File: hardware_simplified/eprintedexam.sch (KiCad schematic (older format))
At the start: 47 parts, among them J1 Conn_01x04, J2 Conn_01x08, Q1 2N7002, Q2 2N7002, Q3 2N7002, Q4 2N7002, Q5 2N7002, Q6 2N7002, SW1 SW_Push, SW2 SW_Push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

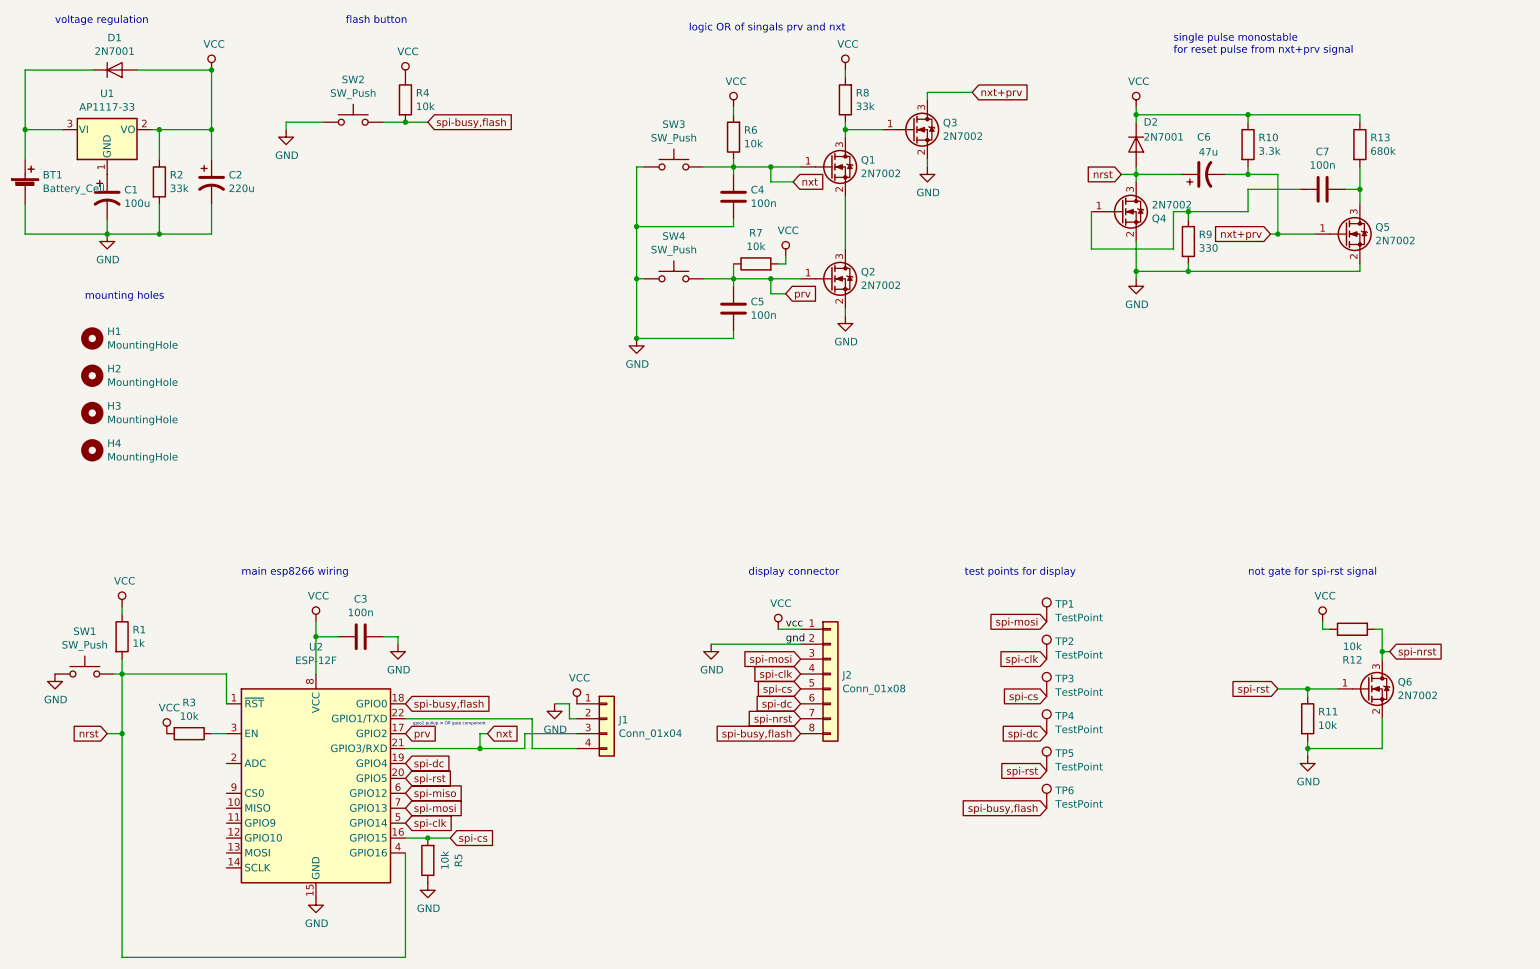
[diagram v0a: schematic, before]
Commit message: fixed monostable and improved pcb layout
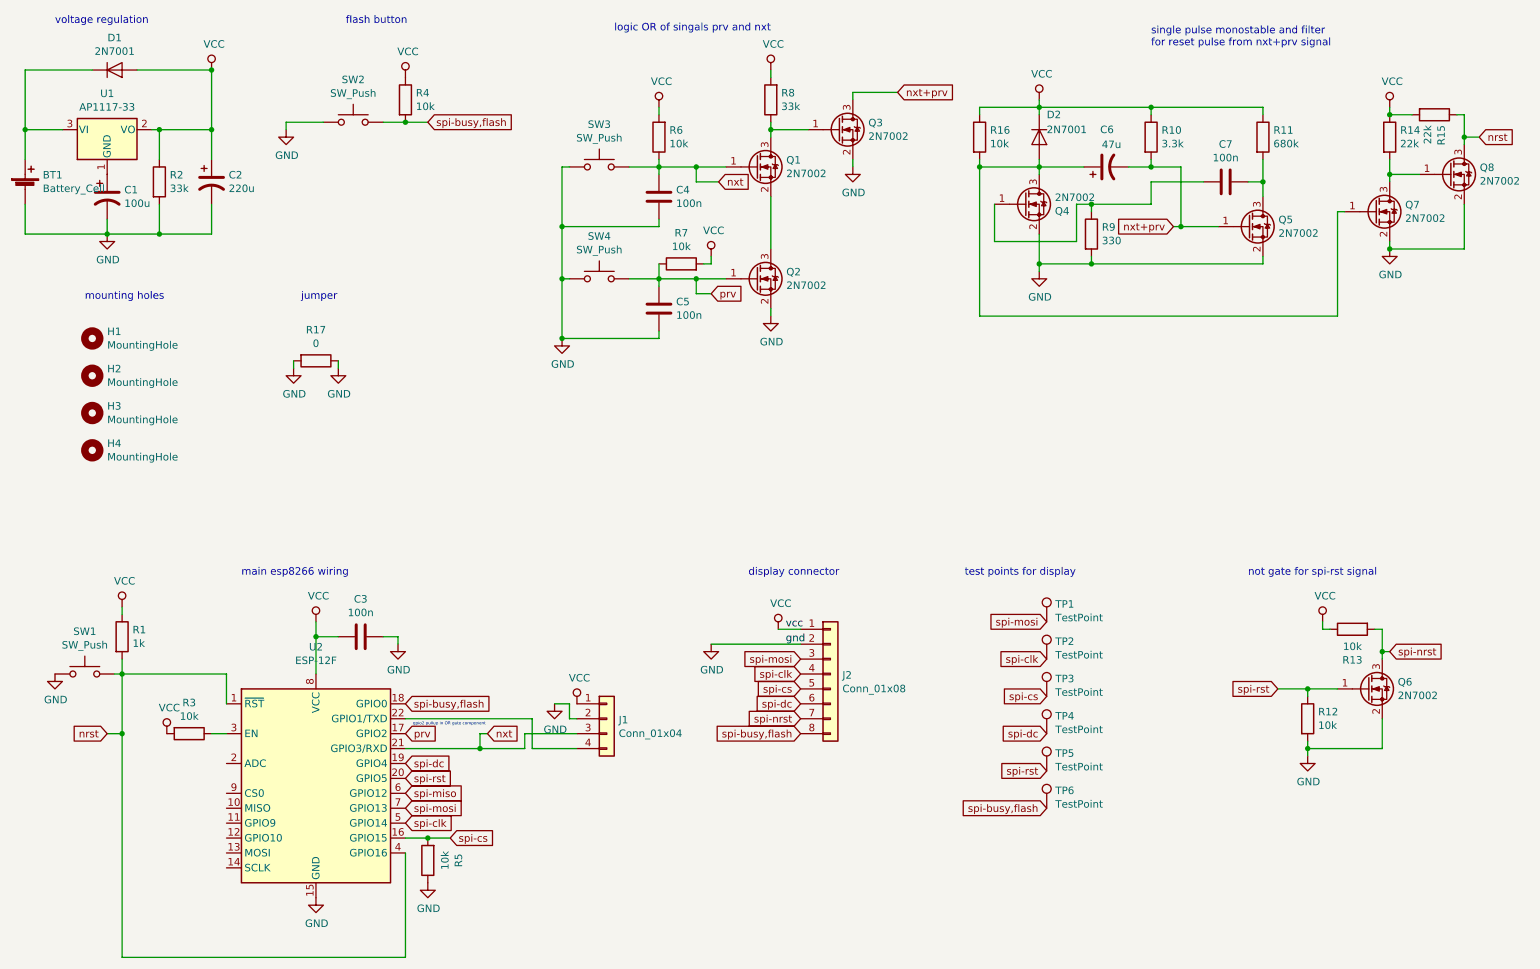
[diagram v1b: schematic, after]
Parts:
- added Q7, Q8: 2N7002, Package_TO_SOT_SMD:SOT-23, symbol Transistor_FET:2N7002
- added R14, R15: 22k, Resistor_SMD:R_1206_3216Metric, symbol Device:R
- added R16: 10k, Resistor_THT:R_Axial_DIN0207_L6.3mm_D2.5mm_P10.16mm_Horizontal, symbol Device:R
- added R17: 0, Resistor_SMD:R_1206_3216Metric, symbol Device:R
- renumbered R13 to R11, R11 to R12, R12 to R13
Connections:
- net GND: now also Q7.2 (S), Q8.2 (S), R17.1, R17.2
- net VCC: now also R14.1, R15.2, R16.1
- net nrst: now also Q8.3 (D), R15.1; no longer C6.1, D2.2 (A), Q4.3 (D)
- new net: C6.1, D2.2 (A), Q4.3 (D), Q7.1 (G), R16.2
- new net: Q7.3 (D), Q8.1 (G), R14.2
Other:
- note added: "jumper"
- note added: "single pulse monostable and filter\nfor reset pulse from nxt+prv signal"
- note removed: "single pulse monostable\nfor reset pulse from nxt+prv signal"
- moved on the sheet: C4, C5, C6, C7, D2, Q1, Q2, Q3, Q4, Q5, R10, R11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

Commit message: changed nxt and prv port
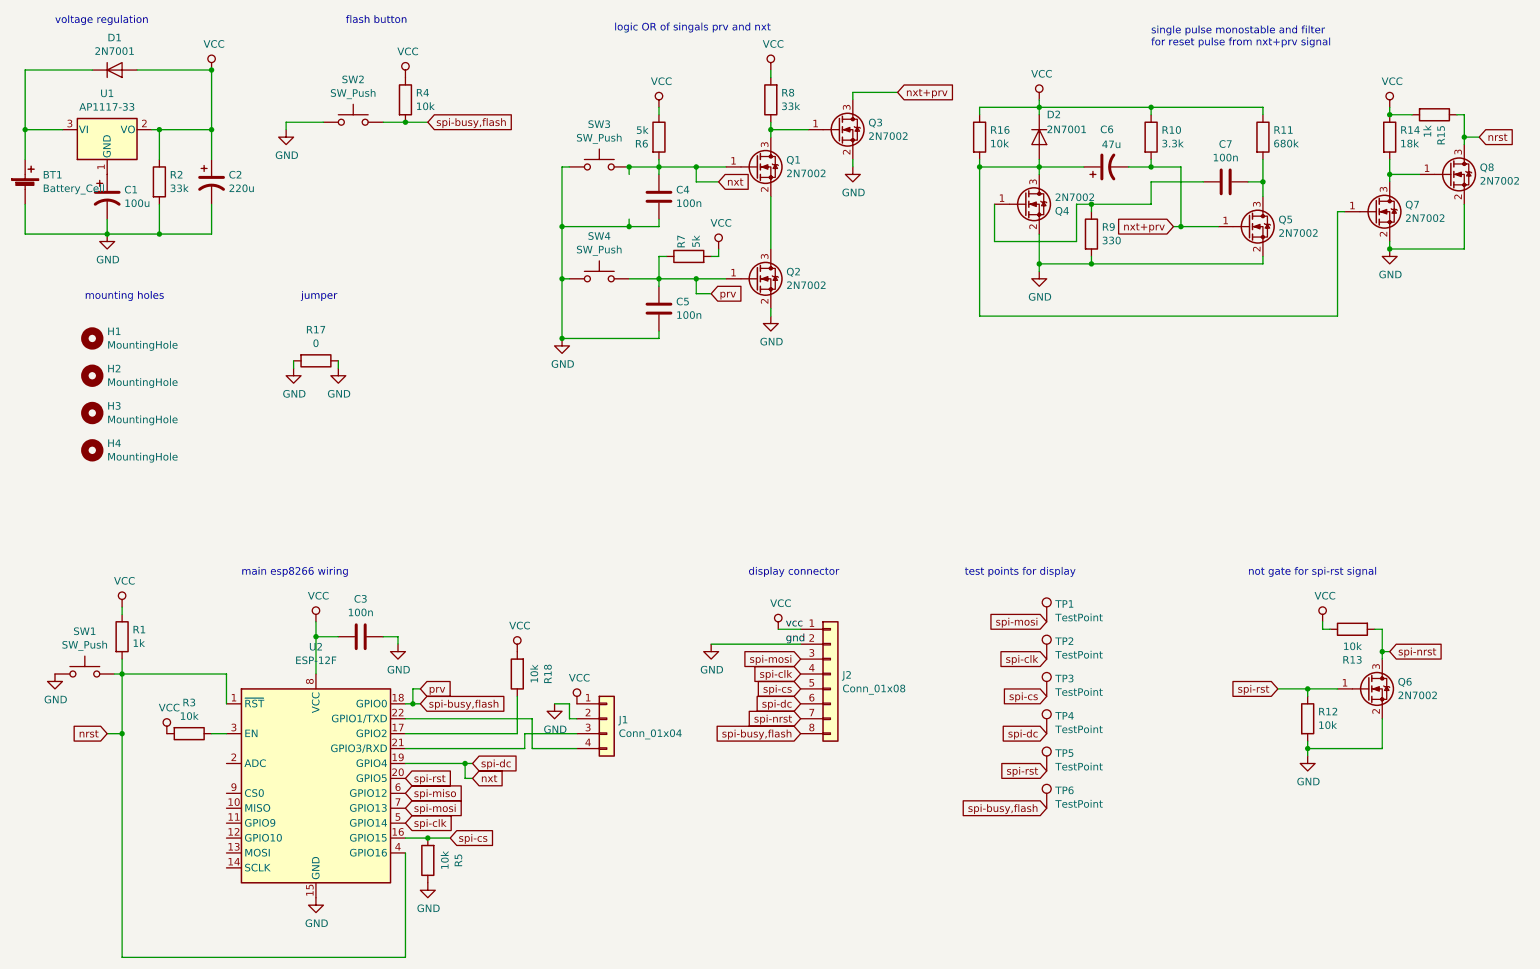
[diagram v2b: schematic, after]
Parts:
- added R18: 10k, Resistor_SMD:R_1206_3216Metric, symbol Device:R
- R14: value 22k -> 18k
- R15: value 22k -> 1k
- R6, R7: value 10k -> 5k
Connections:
- net spi-busy,flash is gone; now on net prv: J2.8 (Pin_8), R4.2, SW2.2, TP6.1, U2.18 (GPIO0)
- net spi-dc is gone; now on net nxt: J2.6 (Pin_6), TP4.1, U2.19 (GPIO4)
- net VCC: now also R6.1, R18.2; no longer R6.2
- net nxt: now also R6.2; no longer J1.3 (Pin_3), R6.1, U2.21 (GPIO3/RXD)
- net prv: no longer U2.17 (GPIO2)
- new net: R18.1, U2.17 (GPIO2)
- new net: J1.3 (Pin_3), U2.21 (GPIO3/RXD)
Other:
- note removed: "gpio2 pullup in OR gate component"
- moved on the sheet: R7
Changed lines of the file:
@@
 Text GLabel 3400 5850 2    50   Input ~ 0
 spi-rst
-Text GLabel 3400 5750 2    50   Input ~ 0
+Text GLabel 3850 5750 2    50   Input ~ 0
 spi-dc
 Text GLabel 3400 6050 2    50   Input ~ 0
@@
 Text GLabel 6050 5050 0    50   Input ~ 0
 spi-mosi
-Text GLabel 3400 5350 2    50   Input ~ 0
+Text GLabel 3500 5350 2    50   Input ~ 0
 spi-busy,flash
 Text GLabel 6050 5350 0    50   Input ~ 0
@@
 Wire Wire Line
 	4500 5450 4550 5450
-Text GLabel 3950 5550 2    50   Input ~ 0
+Text GLabel 3850 5850 2    50   Input ~ 0
 nxt
-Text GLabel 3400 5550 2    50   Input ~ 0
-prv
 Wire Wire Line
 	3400 1450 3550 1450
@@
 P 5100 1550
 F 0 "R6" H 5030 1504 50  0000 R CNN
-F 1 "10k" H 5030 1595 50  0000 R CNN
+F 1 "5k" H 5030 1595 50  0000 R CNN
 F 2 "Resistor_SMD:R_1206_3216Metric" V 5030 1550 50  0001 C CNN
 F 3 "~" H 5100 1550 50  0001 C CNN
 	1    5100 1550
-	-1   0    0    1
+	1    0    0    -1
 $EndComp
 Wire Wire Line
 	5100 1700 5100 1750
 Connection ~ 5100 1750
-$Comp
-L power:VCC #PWR015
-U 1 1 62E44729
-P 5100 1350
-F 0 "#PWR015" H 5100 1200 50  0001 C CNN
-F 1 "VCC" H 5117 1523 50  0000 C CNN
-F 2 "" H 5100 1350 50  0001 C CNN
-F 3 "" H 5100 1350 50  0001 C CNN
-	1    5100 1350
-	1    0    0    -1
-$EndComp
-Wire Wire Line
-	5100 1350 5100 1400
 Wire Wire Line
 	4500 1750 4450 1750
@@
 L Device:R R7
 U 1 1 62E5EEB6
-P 5250 2400
-F 0 "R7" V 5457 2400 50  0000 C CNN
-F 1 "10k" V 5366 2400 50  0000 C CNN
-F 2 "Resistor_SMD:R_1206_3216Metric" V 5180 2400 50  0001 C CNN
-F 3 "~" H 5250 2400 50  0001 C CNN
-	1    5250 2400
+P 5300 2350
+F 0 "R7" H 5400 2400 50  0000 C CNN
+F 1 "5k" H 5400 2300 50  0000 C CNN
+F 2 "Resistor_SMD:R_1206_3216Metric" V 5230 2350 50  0001 C CNN
+F 3 "~" H 5300 2350 50  0001 C CNN
+	1    5300 2350
 	0    -1   -1   0
 $EndComp
 Connection ~ 5100 2500
-$Comp
-L power:VCC #PWR016
-U 1 1 62E5EEBE
-P 5450 2350
-F 0 "#PWR016" H 5450 2200 50  0001 C CNN
-F 1 "VCC" H 5467 2523 50  0000 C CNN
-F 2 "" H 5450 2350 50  0001 C CNN
-F 3 "" H 5450 2350 50  0001 C CNN
-	1    5450 2350
-	1    0    0    -1
-$EndComp
 Wire Wire Line
 	4500 2500 4450 2500
@@
 Wire Wire Line
 	5100 2500 5350 2500
-Wire Wire Line
-	5100 2400 5100 2500
-Wire Wire Line
-	5400 2400 5450 2400
-Wire Wire Line
-	5450 2400 5450 2350
 Connection ~ 4450 2500
 Wire Wire Line
@@
 $EndComp
 Wire Wire Line
-	3400 5650 3900 5650
-Wire Wire Line
-	3950 5550 3900 5550
-Wire Wire Line
-	3900 5550 3900 5650
-Wire Wire Line
 	1400 5550 1500 5550
 Connection ~ 1500 5550
 Wire Wire Line
 	1500 5550 1500 7050
-Text Notes 3450 5500 0    20   ~ 0
-gpio2 pullup in OR gate component
 Wire Wire Line
 	4250 5450 4250 5650
 Wire Wire Line
-	3400 5450 4250 5450
-Wire Wire Line
 	4250 5650 4550 5650
 Wire Wire Line
@@
 Wire Wire Line
 	4200 5550 4550 5550
-Wire Wire Line
-	3900 5650 4200 5650
-Connection ~ 3900 5650
 $Comp
 L Transistor_FET:2N7002 Q6
@@
 Wire Wire Line
 	4900 2500 5100 2500
-Wire Wire Line
-	5100 2900 4450 2900
 Connection ~ 4450 2900
 Wire Wire Line
-	5100 2150 4450 2150
+	5100 2150 4900 2150
 Connection ~ 4450 2150
 Wire Wire Line
@@
 P 10300 1400
 F 0 "R15" H 10370 1446 50  0000 L CNN
-F 1 "22k" H 10370 1355 50  0000 L CNN
+F 1 "1k" H 10370 1355 50  0000 L CNN
 F 2 "Resistor_SMD:R_1206_3216Metric" V 10230 1400 50  0001 C CNN
 F 3 "~" H 10300 1400 50  0001 C CNN
@@
 P 10000 1550
 F 0 "R14" H 10070 1596 50  0000 L CNN
-F 1 "22k" H 10070 1505 50  0000 L CNN
+F 1 "18k" H 10070 1505 50  0000 L CNN
 F 2 "Resistor_SMD:R_1206_3216Metric" V 9930 1550 50  0001 C CNN
 F 3 "~" H 10000 1550 50  0001 C CNN
@@
 Text Notes 2700 2650 0    50   ~ 0
 jumper
+Wire Wire Line
+	4900 1750 4900 1800
+Connection ~ 4900 1750
+Wire Wire Line
+	4900 2100 4900 2150
+Connection ~ 4900 2150
+Wire Wire Line
+	4900 2150 4450 2150
+Wire Wire Line
+	3400 5650 4200 5650
+Wire Wire Line
+	3850 5750 3800 5750
+Wire Wire Line
+	3800 5750 3800 5850
+Wire Wire Line
+	3800 5850 3850 5850
+Text GLabel 3500 5250 2    50   Input ~ 0
+prv
+Wire Wire Line
+	3400 5350 3450 5350
+Wire Wire Line
+	3450 5350 3450 5250
+Wire Wire Line
+	3450 5250 3500 5250
+Connection ~ 3450 5350
+Wire Wire Line
+	3450 5350 3500 5350
+$Comp
+L Device:R R18
+U 1 1 62DCA654
+P 4150 5150
+F 0 "R18" V 3943 5150 50  0000 C CNN
+F 1 "10k" V 4034 5150 50  0000 C CNN
+F 2 "Resistor_SMD:R_1206_3216Metric" V 4080 5150 50  0001 C CNN
+F 3 "~" H 4150 5150 50  0001 C CNN
+	1    4150 5150
+	-1   0    0    1
+$EndComp
+Wire Wire Line
+	3400 5550 4150 5550
+Wire Wire Line
+	4150 5550 4150 5300
+$Comp
+L power:VCC #PWR0103
+U 1 1 62E88E6E
+P 4150 5000
+F 0 "#PWR0103" H 4150 4850 50  0001 C CNN
+F 1 "VCC" H 4167 5173 50  0000 C CNN
+F 2 "" H 4150 5000 50  0001 C CNN
+F 3 "" H 4150 5000 50  0001 C CNN
+	1    4150 5000
+	1    0    0    -1
+$EndComp
+Wire Wire Line
+	4450 2900 5100 2900
+Wire Wire Line
+	5100 2500 5100 2350
+Wire Wire Line
+	5100 2350 5150 2350
+$Comp
+L power:VCC #PWR0104
+U 1 1 62EA6C90
+P 5100 1350
+F 0 "#PWR0104" H 5100 1200 50  0001 C CNN
+F 1 "VCC" H 5117 1523 50  0000 C CNN
+F 2 "" H 5100 1350 50  0001 C CNN
+F 3 "" H 5100 1350 50  0001 C CNN
+	1    5100 1350
+	1    0    0    -1
+$EndComp
+$Comp
+L power:VCC #PWR0105
+U 1 1 62EA8111
+P 5500 2300
+F 0 "#PWR0105" H 5500 2150 50  0001 C CNN
+F 1 "VCC" H 5517 2473 50  0000 C CNN
+F 2 "" H 5500 2300 50  0001 C CNN
+F 3 "" H 5500 2300 50  0001 C CNN
+	1    5500 2300
+	1    0    0    -1
+$EndComp
+Wire Wire Line
+	5450 2350 5500 2350
+Wire Wire Line
+	5500 2350 5500 2300
+Wire Wire Line
+	5100 1350 5100 1400
+Wire Wire Line
+	3400 5450 4250 5450
+Connection ~ 3800 5750
+Wire Wire Line
+	3800 5750 3400 5750
 $EndSCHEMATC
